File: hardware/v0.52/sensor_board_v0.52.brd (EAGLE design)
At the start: 55.2 x 39.9 mm, 48 parts, among them J3 USB-MICROB, U1 ATMEGA328P, U2 TSL2561, U3 OPA344, U4 RFM69HW, U5 FT231XS, U6 ADMP401, U7 SHT31-DIS, U8 MCP1703CB, U9 BMP280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

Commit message: Added fiducial markers on PCB
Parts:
- added U$1, U$2, U$3: FIDUCIAL, adafruit:FIDUCIAL_1MM
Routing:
- net GND: vias 73 -> 71
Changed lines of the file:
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@@
 <text x="36.576" y="9.9568" size="1.016" layer="122" font="vector" ratio="16" rot="MR0" align="center-left">Touchstone</text>
 <text x="32.258" y="7.112" size="0.6096" layer="121" font="vector">Designed by Akram Ali and Dave Conroy</text>
-<text x="54.0258" y="16.5354" size="0.6096" layer="121" font="vector" rot="R90" align="bottom-center">v0.52
+<text x="54.3814" y="18.8214" size="0.6096" layer="121" font="vector" rot="R90" align="bottom-center">v0.52
 February 2017</text>
-<text x="54.5084" y="20.066" size="0.8128" layer="121" font="vector" ratio="12" rot="R270">crtlabs.org</text>
+<text x="54.7624" y="22.352" size="0.8128" layer="121" font="vector" ratio="12" rot="R270">crtlabs.org</text>
 <rectangle x1="43.4594" y1="8.001" x2="43.8658" y2="8.0518" layer="122" rot="R180"/>
 <rectangle x1="43.4086" y1="8.0518" x2="43.9674" y2="8.1026" layer="122" rot="R180"/>
@@
 <element name="J3" library="SparkFun-Connectors" package="USB-MICROB" value="USB-MICROB" x="29.3624" y="45.0088" smashed="yes" rot="R180">
 <attribute name="PROD_ID" value="CONN-09505" x="29.3624" y="45.0088" size="1.778" layer="27" rot="R180" display="off"/>
-<attribute name="NAME" x="34.2644" y="43.4792" size="0.6096" layer="121" font="vector" rot="R180"/>
+<attribute name="NAME" x="25.6284" y="43.6316" size="0.6096" layer="121" font="vector" rot="R180"/>
 </element>
 <element name="U5" library="SparkFun-DigitalIC" package="SSOP20_L" value="FT231XS" x="18.6436" y="41.9608" smashed="yes">
@@
 <attribute name="VALUE" x="2.794" y="5.7658" size="1.27" layer="27"/>
 </element>
+<element name="U$1" library="adafruit" package="FIDUCIAL_1MM" value="FIDUCIAL" x="54.864" y="13.3096"/>
+<element name="U$2" library="adafruit" package="FIDUCIAL_1MM" value="FIDUCIAL" x="3.8608" y="39.8272"/>
+<element name="U$3" library="adafruit" package="FIDUCIAL_1MM" value="FIDUCIAL" x="34.544" y="42.0624"/>
 </elements>
 <signals>
@@
 <wire x1="52.5982" y1="35.4786" x2="51.9684" y2="34.8488" width="0.1778" layer="1"/>
 <wire x1="51.9684" y1="34.8488" x2="51.9684" y2="33.7312" width="0.1778" layer="1"/>
-<via x="24.3332" y="42.7228" extent="1-16" drill="0.254" diameter="0.127"/>
+<via x="24.1808" y="42.7228" extent="1-16" drill="0.254" diameter="0.127"/>
 <via x="25.4508" y="41.3512" extent="1-16" drill="0.254" diameter="0.127"/>
 <via x="26.7208" y="42.2148" extent="1-16" drill="0.254" diameter="0.127"/>
 <via x="31.6992" y="41.3512" extent="1-16" drill="0.254" diameter="0.127"/>
-<via x="33.1724" y="41.7576" extent="1-16" drill="0.254" diameter="0.127"/>
 <via x="3.556" y="14.8336" extent="1-16" drill="0.254" diameter="0.127"/>
 <via x="17.272" y="19.5072" extent="1-16" drill="0.254" diameter="0.127"/>
@@
 <via x="8.89" y="27.7368" extent="1-16" drill="0.254" diameter="0.127"/>
 <via x="5.6388" y="37.6428" extent="1-16" drill="0.254" diameter="0.127"/>
-<via x="3.556" y="40.3352" extent="1-16" drill="0.254" diameter="0.127"/>
 <via x="28.575" y="12.192" extent="1-16" drill="0.254" diameter="0.127"/>
 <via x="26.67" y="12.192" extent="1-16" drill="0.254" diameter="0.127"/>

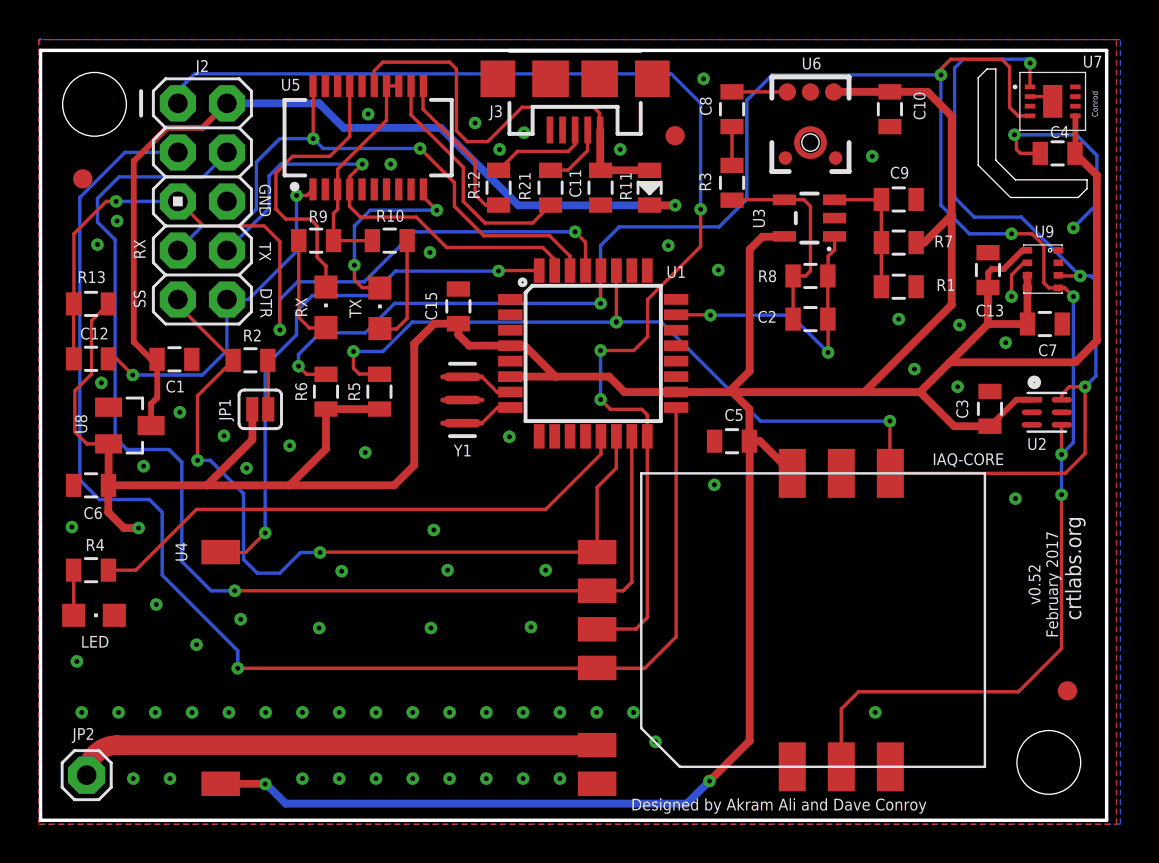
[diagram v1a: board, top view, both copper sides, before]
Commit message: Some trace adjustments
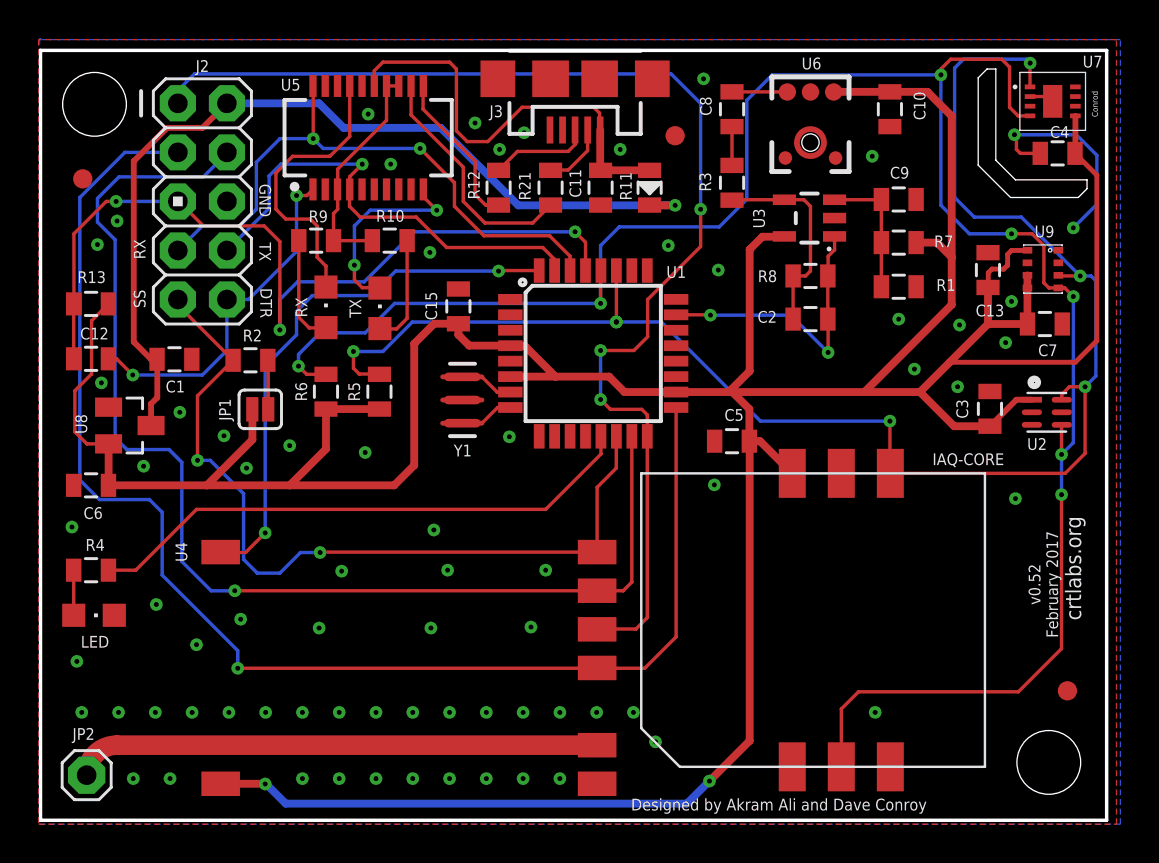
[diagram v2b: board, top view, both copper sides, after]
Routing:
- net VCC: track 208.4 -> 205.2 mm, vias 3 -> 2
- net GND: track 14.6 -> 12.4 mm
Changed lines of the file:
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@@
 <wire x1="52.927" y1="44.0904" x2="53.852" y2="44.0904" width="0.1778" layer="1"/>
 <wire x1="53.852" y1="44.0904" x2="54.102" y2="43.8404" width="0.1778" layer="1"/>
-<via x="51.9684" y="33.7312" extent="1-16" drill="0.254" diameter="0.127"/>
 <via x="51.6636" y="31.3436" extent="1-16" drill="0.254" diameter="0.127"/>
-<wire x1="52.794" y1="35.4786" x2="52.5982" y2="35.4786" width="0.1778" layer="1"/>
-<wire x1="52.5982" y1="35.4786" x2="51.9684" y2="34.8488" width="0.1778" layer="1"/>
-<wire x1="51.9684" y1="34.8488" x2="51.9684" y2="33.7312" width="0.1778" layer="1"/>
 <via x="24.1808" y="42.7228" extent="1-16" drill="0.254" diameter="0.127"/>
 <via x="25.4508" y="41.3512" extent="1-16" drill="0.254" diameter="0.127"/>
@@
 <via x="8.382" y="8.763" extent="1-16" drill="0.254" diameter="0.127"/>
 <via x="6.477" y="8.763" extent="1-16" drill="0.254" diameter="0.127"/>
+<via x="51.9684" y="33.4772" extent="1-16" drill="0.254" diameter="0.127"/>
 </signal>
 <signal name="VCC">
@@
 <wire x1="16.4592" y1="25.8318" x2="16.4592" y2="27.9036" width="0.4064" layer="1"/>
 <wire x1="16.4592" y1="25.8318" x2="14.5796" y2="23.9522" width="0.4064" layer="1"/>
-<via x="6.7564" y="21.7424" extent="1-16" drill="0.254" diameter="0.127"/>
-<wire x1="6.7564" y1="21.7424" x2="5.9944" y2="21.7424" width="0.4064" layer="1"/>
-<wire x1="5.9944" y1="21.7424" x2="5.1816" y2="22.5552" width="0.4064" layer="1"/>
-<wire x1="5.1816" y1="22.5552" x2="5.1816" y2="23.9412" width="0.4064" layer="1"/>
 <wire x1="5.1816" y1="23.9412" x2="5.1926" y2="23.9522" width="0.4064" layer="1"/>
 <wire x1="23.3172" y1="32.3232" x2="22.0616" y2="32.3232" width="0.4064" layer="1"/>
@@
 <wire x1="44.3484" y1="28.7848" x2="47.2252" y2="28.7848" width="0.4064" layer="1"/>
 <wire x1="50.8398" y1="27.0256" x2="50.8508" y2="27.0146" width="0.4064" layer="1"/>
-<wire x1="38.3904" y1="26.2382" x2="38.3904" y2="27.9036" width="0.4064" layer="1"/>
 <wire x1="38.3904" y1="27.9036" x2="37.4142" y2="28.8798" width="0.4064" layer="1"/>
 <wire x1="38.3904" y1="26.2382" x2="38.9458" y2="26.2382" width="0.4064" layer="1"/>
@@
 <wire x1="50.7636" y1="34.1884" x2="50.7492" y2="34.2028" width="0.4064" layer="1"/>
 <wire x1="47.2252" y1="28.7848" x2="48.768" y2="30.3276" width="0.4064" layer="1"/>
-<wire x1="48.768" y1="30.3276" x2="55.2704" y2="30.3276" width="0.4064" layer="1"/>
-<wire x1="55.2704" y1="30.3276" x2="56.388" y2="31.4452" width="0.4064" layer="1"/>
-<wire x1="56.388" y1="31.4452" x2="56.388" y2="40.016" width="0.4064" layer="1"/>
-<wire x1="56.388" y1="40.016" x2="55.256" y2="41.148" width="0.4064" layer="1"/>
+<wire x1="48.768" y1="30.3276" x2="55.2704" y2="30.3276" width="0.254" layer="1"/>
+<wire x1="55.2704" y1="30.3276" x2="56.388" y2="31.4452" width="0.254" layer="1"/>
+<wire x1="56.388" y1="31.4452" x2="56.388" y2="40.016" width="0.254" layer="1"/>
+<wire x1="56.388" y1="40.016" x2="55.256" y2="41.148" width="0.254" layer="1"/>
 <wire x1="55.277" y1="43.0904" x2="55.277" y2="41.169" width="0.3048" layer="1"/>
 <wire x1="55.277" y1="41.169" x2="55.256" y2="41.148" width="0.3048" layer="1"/>
@@
 <wire x1="45.6692" y1="44.334" x2="47.614" y2="44.334" width="0.4064" layer="1"/>
 <wire x1="47.614" y1="44.334" x2="48.8696" y2="43.0784" width="0.4064" layer="1"/>
-<wire x1="48.8696" y1="43.0784" x2="48.8696" y2="37.9476" width="0.4064" layer="1"/>
-<wire x1="48.8696" y1="37.9476" x2="48.8696" y2="33.306" width="0.4064" layer="1"/>
+<wire x1="48.8696" y1="43.0784" x2="48.8696" y2="35.7632" width="0.4064" layer="1"/>
+<wire x1="48.8696" y1="35.7632" x2="48.8696" y2="33.306" width="0.4064" layer="1"/>
 <wire x1="48.8696" y1="33.306" x2="44.3484" y2="28.7848" width="0.4064" layer="1"/>
-<wire x1="47.0264" y1="36.5252" x2="47.4472" y2="36.5252" width="0.4064" layer="1"/>
-<wire x1="47.4472" y1="36.5252" x2="48.8696" y2="37.9476" width="0.4064" layer="1"/>
 <wire x1="45.6692" y1="44.334" x2="42.7616" y2="44.334" width="0.4064" layer="1"/>
 <wire x1="42.7616" y1="44.334" x2="42.7544" y2="44.3268" width="0.4064" layer="1"/>
@@
 <wire x1="53.0222" y1="28.3868" x2="52.223" y2="28.3868" width="0.3048" layer="1"/>
 <wire x1="52.223" y1="28.3868" x2="50.8508" y2="27.0146" width="0.3048" layer="1"/>
-<wire x1="50.7636" y1="34.1884" x2="50.7636" y2="34.9648" width="0.3048" layer="1"/>
-<wire x1="50.7636" y1="34.9648" x2="50.9524" y2="35.1536" width="0.3048" layer="1"/>
-<wire x1="50.9524" y1="35.1536" x2="51.562" y2="35.1536" width="0.3048" layer="1"/>
-<wire x1="52.7842" y1="36.1188" x2="52.794" y2="36.1286" width="0.3048" layer="1"/>
-<wire x1="52.7842" y1="36.1188" x2="52.5272" y2="36.1188" width="0.3048" layer="1"/>
-<wire x1="52.5272" y1="36.1188" x2="51.562" y2="35.1536" width="0.3048" layer="1"/>
+<wire x1="50.7636" y1="34.1884" x2="50.7636" y2="34.9648" width="0.254" layer="1"/>
+<wire x1="50.7636" y1="34.9648" x2="50.9524" y2="35.1536" width="0.254" layer="1"/>
 <wire x1="4.318" y1="32.4756" x2="4.318" y2="29.718" width="0.1778" layer="1"/>
 <wire x1="4.318" y1="29.718" x2="3.4544" y2="28.8544" width="0.1778" layer="1"/>
@@
 <wire x1="36.322" y1="8.636" x2="35.1536" y2="7.4676" width="0.4064" layer="16"/>
 <wire x1="35.1536" y1="7.4676" x2="14.3764" y2="7.4676" width="0.4064" layer="16"/>
+<wire x1="50.9524" y1="35.1536" x2="51.562" y2="35.1536" width="0.254" layer="1"/>
+<wire x1="51.562" y1="35.1536" x2="51.7652" y2="35.3568" width="0.254" layer="1"/>
+<wire x1="51.7652" y1="35.3568" x2="51.7652" y2="35.9156" width="0.254" layer="1"/>
+<wire x1="51.7652" y1="35.9156" x2="51.9684" y2="36.1188" width="0.254" layer="1"/>
+<wire x1="51.9684" y1="36.1188" x2="52.7842" y2="36.1188" width="0.254" layer="1"/>
+<wire x1="52.7842" y1="36.1188" x2="52.794" y2="36.1286" width="0.254" layer="1"/>
+<wire x1="47.0264" y1="36.5252" x2="48.1076" y2="36.5252" width="0.4064" layer="1"/>
+<wire x1="48.1076" y1="36.5252" x2="48.8696" y2="35.7632" width="0.4064" layer="1"/>
+<wire x1="38.3904" y1="26.2382" x2="38.3904" y2="27.9036" width="0.4064" layer="1"/>
 </signal>
 <signal name="SCL">
